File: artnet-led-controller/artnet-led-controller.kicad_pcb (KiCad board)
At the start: 2 copper layers, 100 x 70 mm, 84 parts, among them J1 USB4125-GF-A, J10 SWD_DEBUG, J2 HR911105A, J3 VBAT JST-PH-2, J5 LED_OUT_1, J6 LED_OUT_2, J7 LED_OUT_3, J8 LED_OUT_4, J9 OLED_SSD1306, SW1 SW_Push, SW2 SW_Push, SW3 SW_Push, SW4 SW_Push, U1 RP2354A, U3 W5500, U4 SN74AHCT125, U5 TP4056, U6 MT3608, U7 AMS1117-3.3, Y1 12MHz, Y2 25MHz

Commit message: Add netlist extraction and PCB pad net assignment
gen_schematic.py now exports netlist.json mapping each ref to its
pad-to-net assignments. gen_pcb.py loads this and injects (net N "name")
into every pad block so the board is routable with freerouting.
Also fixes pin_ep sign bug (cy+py -> cy-py) in schematic generator.

Co-Authored-By: Claude Sonnet 4.6 <noreply@anthropic.com>
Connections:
- C10 pad 1: (no net) -> GND
- C10 pad 2: (no net) -> VREG_1V1
- C2 pad 1: (no net) -> GND
- C2 pad 2: (no net) -> RP_XIN
- C3 pad 1: (no net) -> GND
- C3 pad 2: (no net) -> RP_XOUT
- C31 pad 1: (no net) -> VUSB
- C31 pad 2: (no net) -> GND
- C32 pad 1: (no net) -> VUSB
- C32 pad 2: (no net) -> GND
- C33 pad 1: (no net) -> VBAT
- C33 pad 2: (no net) -> GND
- C34 pad 1: (no net) -> VCC5V
- C34 pad 2: (no net) -> GND
- C35 pad 1: (no net) -> VCC5V
- C35 pad 2: (no net) -> GND
- C36 pad 1: (no net) -> VCC3V3
- C36 pad 2: (no net) -> GND
- C37 pad 1: (no net) -> VCC3V3
- C37 pad 2: (no net) -> GND
- C38 pad 1: (no net) -> VCC3V3
- C38 pad 2: (no net) -> GND
- C39 pad 1: (no net) -> VCC3V3
- C39 pad 2: (no net) -> GND
- C4 pad 1: (no net) -> GND
- C4 pad 2: (no net) -> W5_VDD
- C40 pad 1: (no net) -> VCC3V3
- C40 pad 2: (no net) -> GND
- C41 pad 1: (no net) -> VCC3V3
- C41 pad 2: (no net) -> GND
- C42 pad 1: (no net) -> VCC3V3
- C42 pad 2: (no net) -> GND
- C43 pad 1: (no net) -> VCC3V3
- C43 pad 2: (no net) -> GND
- C44 pad 1: (no net) -> VCC3V3
- C44 pad 2: (no net) -> GND
- C45 pad 1: (no net) -> VCC3V3
- C45 pad 2: (no net) -> GND
- C46 pad 1: (no net) -> VCC3V3
- C46 pad 2: (no net) -> GND
- C47 pad 1: (no net) -> VCC3V3
- C47 pad 2: (no net) -> GND
- C48 pad 1: (no net) -> VCC3V3
- C48 pad 2: (no net) -> GND
- C49 pad 1: (no net) -> VCC3V3
- C49 pad 2: (no net) -> GND
- C5 pad 1: (no net) -> GND
- C5 pad 2: (no net) -> W5_XTAL1
- C50 pad 1: (no net) -> VCC3V3
- C50 pad 2: (no net) -> GND
- C51 pad 1: (no net) -> VCC3V3
- C51 pad 2: (no net) -> GND
- C52 pad 1: (no net) -> VCC5V
- C52 pad 2: (no net) -> GND
- C6 pad 1: (no net) -> GND
- C6 pad 2: (no net) -> W5_XTAL2
- C7 pad 1: (no net) -> GND
- C7 pad 2: (no net) -> VREG_1V1
- C8 pad 1: (no net) -> GND
- C8 pad 2: (no net) -> VREG_AVDD
- C9 pad 1: (no net) -> GND
- C9 pad 2: (no net) -> VREG_1V1
- D1 pad 1: (no net) -> VCC5V
- D1 pad 2: (no net) -> VBOOST_RAW
- D2 pad 1: (no net) -> GND
- D2 pad 2: (no net) -> CHRG_STAT
- J1 pad A12: (no net) -> GND
- J1 pad A5: (no net) -> USB_CC1
- J1 pad B12: (no net) -> GND
- J1 pad B5: (no net) -> USB_CC2
- J10 pad 1: (no net) -> SWCLK
- J10 pad 2: (no net) -> SWDIO
- J10 pad 3: (no net) -> GND
- J2 pad 11: (no net) -> ETH_TXP
- J2 pad 12: (no net) -> ETH_TXN
- J2 pad 4: (no net) -> GND
- J2 pad 5: (no net) -> GND
- J2 pad 7: (no net) -> VCC3V3
- J2 pad 8: (no net) -> ETH_CT1
- J2 pad 9: (no net) -> ETH_CT2
- J3 pad 1: (no net) -> VBAT
- J3 pad 2: (no net) -> GND
- J5 pad 1: (no net) -> GND
- J5 pad 2: (no net) -> LED1_DATA_5V
- J5 pad 3: (no net) -> VCC5V
- J6 pad 1: (no net) -> GND
- J6 pad 2: (no net) -> LED2_DATA_5V
- J6 pad 3: (no net) -> VCC5V
- J7 pad 1: (no net) -> GND
- J7 pad 2: (no net) -> LED3_DATA_5V
- J7 pad 3: (no net) -> VCC5V
- J8 pad 1: (no net) -> GND
- J8 pad 2: (no net) -> LED4_DATA_5V
- J8 pad 3: (no net) -> VCC5V
- J9 pad 1: (no net) -> VCC3V3
- J9 pad 2: (no net) -> GND
- J9 pad 3: (no net) -> I2C_SCL
- J9 pad 4: (no net) -> I2C_SDA
- L1 pad 1: (no net) -> VBOOST_RAW
- L1 pad 2: (no net) -> MT3608_SW
- L2 pad 1: (no net) -> VREG_1V1
- L2 pad 2: (no net) -> VREG_LX
- R1 pad 1: (no net) -> MT3608_FB
- R1 pad 2: (no net) -> VCC5V
- R10 pad 1: (no net) -> USB_DM_MCU
- R10 pad 2: (no net) -> USB_DM
- R11 pad 1: (no net) -> GND
- R11 pad 2: (no net) -> W5500_EXRES0
- R12 pad 1: (no net) -> GND
- R12 pad 2: (no net) -> W5500_RCLK
- R13 pad 1: (no net) -> W5500_EXRES1
- R13 pad 2: (no net) -> VCC3V3
- R14 pad 1: (no net) -> SPI_MISO
- R14 pad 2: (no net) -> VCC3V3
- R15 pad 1: (no net) -> SPI_CS
- R15 pad 2: (no net) -> VCC3V3
- R16 pad 1: (no net) -> W5500_RST
- R16 pad 2: (no net) -> VCC3V3
- R17 pad 1: (no net) -> ETH_CT1
- R17 pad 2: (no net) -> VCC3V3
- R18 pad 1: (no net) -> ETH_CT2
- R18 pad 2: (no net) -> VCC3V3
- R19 pad 1: (no net) -> I2C_SCL
- R19 pad 2: (no net) -> VCC3V3
- R2 pad 1: (no net) -> GND
- R2 pad 2: (no net) -> MT3608_FB
- R20 pad 1: (no net) -> I2C_SDA
- R20 pad 2: (no net) -> VCC3V3
- R21 pad 1: (no net) -> BTN1
- R21 pad 2: (no net) -> VCC3V3
- R22 pad 1: (no net) -> BTN2
- R22 pad 2: (no net) -> VCC3V3
- R23 pad 1: (no net) -> VREG_AVDD
- R23 pad 2: (no net) -> VCC3V3
- R24 pad 1: (no net) -> USB_BOOT_SW
- R24 pad 2: (no net) -> USB_BOOT
- R3 pad 1: (no net) -> GND
- R3 pad 2: (no net) -> TP4056_PROG
- R4 pad 1: (no net) -> GND
- R4 pad 2: (no net) -> USB_CC1
- R5 pad 1: (no net) -> GND
- R5 pad 2: (no net) -> USB_CC2
- R6 pad 2: (no net) -> CHRG_STAT
- R7 pad 1: (no net) -> CHRG_STAT
- R7 pad 2: (no net) -> VCC3V3
- R8 pad 1: (no net) -> RP_RUN
- R8 pad 2: (no net) -> VCC3V3
- R9 pad 1: (no net) -> USB_DP_MCU
- R9 pad 2: (no net) -> USB_DP
- SW1 pad 1: (no net) -> BTN1
- SW1 pad 2: (no net) -> GND
- SW2 pad 1: (no net) -> BTN2
- SW2 pad 2: (no net) -> GND
- SW3 pad 1: (no net) -> RP_RUN
- SW3 pad 2: (no net) -> GND
- SW4 pad 1: (no net) -> USB_BOOT_SW
- SW4 pad 2: (no net) -> GND
- U1 pad 1: (no net) -> VCC3V3
- U1 pad 11: (no net) -> VCC3V3
- U1 pad 2: (no net) -> LED1_DATA_3V3
- U1 pad 20: (no net) -> VCC3V3
- U1 pad 21: (no net) -> RP_XIN
- U1 pad 22: (no net) -> RP_XOUT
- U1 pad 23: (no net) -> VREG_1V1
- U1 pad 24: (no net) -> SWCLK
- U1 pad 25: (no net) -> SWDIO
- U1 pad 26: (no net) -> RP_RUN
- U1 pad 27: (no net) -> SPI_MISO
- U1 pad 28: (no net) -> SPI_CS
- U1 pad 29: (no net) -> SPI_SCK
- U1 pad 3: (no net) -> LED2_DATA_3V3
- U1 pad 30: (no net) -> VCC3V3
- U1 pad 31: (no net) -> SPI_MOSI
- U1 pad 32: (no net) -> W5500_INT
- U1 pad 33: (no net) -> W5500_RST
- U1 pad 34: (no net) -> BTN1
- U1 pad 35: (no net) -> BTN2
- U1 pad 38: (no net) -> VCC3V3
- U1 pad 39: (no net) -> VREG_1V1
- U1 pad 4: (no net) -> LED3_DATA_3V3
- U1 pad 44: (no net) -> VCC3V3
- U1 pad 45: (no net) -> VCC3V3
- U1 pad 46: (no net) -> VREG_AVDD
- U1 pad 47: (no net) -> GND
- U1 pad 48: (no net) -> VREG_LX
- U1 pad 49: (no net) -> VCC3V3
- U1 pad 5: (no net) -> LED4_DATA_3V3
- U1 pad 50: (no net) -> VREG_1V1
- U1 pad 51: (no net) -> USB_DM_MCU
- U1 pad 52: (no net) -> USB_DP_MCU
- U1 pad 53: (no net) -> VCC3V3
- U1 pad 54: (no net) -> VCC3V3
- U1 pad 6: (no net) -> VREG_1V1
- U1 pad 60: (no net) -> USB_BOOT
- U1 pad 61: (no net) -> GND
- U1 pad 7: (no net) -> I2C_SDA
- U1 pad 8: (no net) -> I2C_SCL
- U3 pad 10: (no net) -> W5500_EXRES0
- U3 pad 11: (no net) -> ETH_TXP
- U3 pad 12: (no net) -> ETH_TXN
- U3 pad 13: (no net) -> ETH_RXN
- U3 pad 14: (no net) -> ETH_RXP
- U3 pad 15: (no net) -> W5_XTAL1
- U3 pad 16: (no net) -> W5_XTAL2
- U3 pad 19: (no net) -> VCC3V3
- U3 pad 20: (no net) -> VCC3V3
- U3 pad 21: (no net) -> SPI_MISO
- U3 pad 22: (no net) -> SPI_MOSI
- U3 pad 23: (no net) -> SPI_SCK
- U3 pad 24: (no net) -> SPI_CS
- U3 pad 25: (no net) -> VCC3V3
- U3 pad 26: (no net) -> W5_VDD
- U3 pad 27: (no net) -> W5500_INT
- U3 pad 28: (no net) -> W5500_RST
- U3 pad 32: (no net) -> GND
- U3 pad 5: (no net) -> W5500_EXRES1
- U3 pad 6: (no net) -> W5500_EXRES1
- U3 pad 7: (no net) -> VCC3V3
- U3 pad 8: (no net) -> GND
- U3 pad 9: (no net) -> W5500_RCLK
- U4 pad 1: (no net) -> GND
- U4 pad 10: (no net) -> LED3_DATA_3V3
- U4 pad 11: (no net) -> LED4_DATA_5V
- U4 pad 12: (no net) -> GND
- U4 pad 13: (no net) -> LED4_DATA_3V3
- U4 pad 14: (no net) -> VCC5V
- U4 pad 2: (no net) -> LED1_DATA_3V3
- U4 pad 3: (no net) -> LED1_DATA_5V
- U4 pad 4: (no net) -> GND
- U4 pad 5: (no net) -> LED2_DATA_3V3
- U4 pad 6: (no net) -> LED2_DATA_5V
- U4 pad 7: (no net) -> GND
- U4 pad 8: (no net) -> LED3_DATA_5V
- U4 pad 9: (no net) -> GND
- U5 pad 1: (no net) -> GND
- U5 pad 2: (no net) -> TP4056_PROG
- U5 pad 3: (no net) -> GND
- U5 pad 4: (no net) -> VUSB
- U5 pad 5: (no net) -> VBAT
- U5 pad 6: (no net) -> CHRG_STAT
- U5 pad 7: (no net) -> STDBY_STAT
- U5 pad 8: (no net) -> VUSB
- U6 pad 1: (no net) -> VBAT
- U6 pad 2: (no net) -> GND
- U6 pad 3: (no net) -> VCC5V
- U6 pad 4: (no net) -> MT3608_FB
- U6 pad 5: (no net) -> MT3608_SW
- U7 pad 1: (no net) -> GND
- U7 pad 2: (no net) -> VCC3V3
- U7 pad 3: (no net) -> VCC5V
- Y1 pad 1: (no net) -> RP_XIN
- Y1 pad 2: (no net) -> RP_XOUT
- Y2 pad 1: (no net) -> W5_XTAL1
- Y2 pad 2: (no net) -> W5_XTAL2

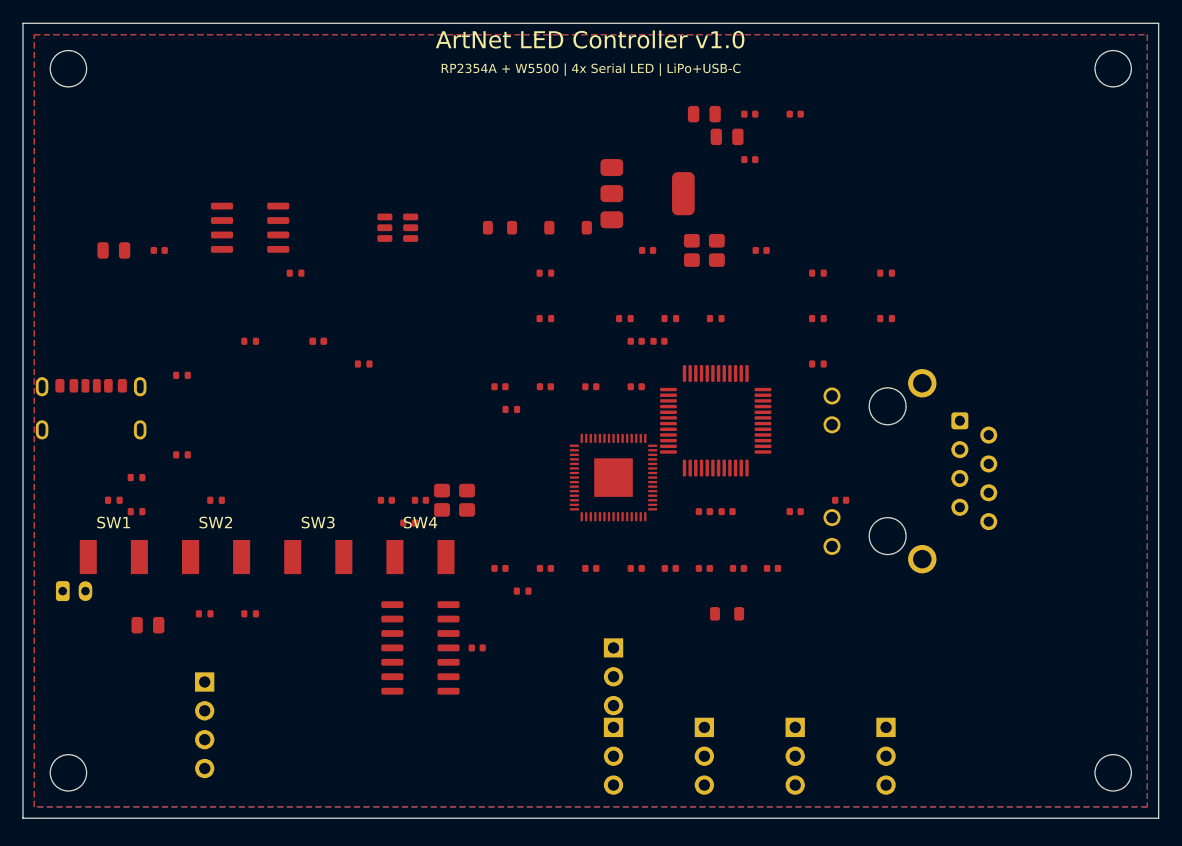
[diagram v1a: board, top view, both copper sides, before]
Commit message: Switch to 4-layer stackup with inner GND and VCC planes
Move to a 4-layer JLCPCB stackup: F.Cu/B.Cu for signals, In1.Cu as
VCC3V3 plane with a VCC5V island over the power-input column, In2.Cu
as a solid GND plane. Reworked component placement (edge-facing jacks,
courtyard-safe clusters) to improve routability.

Freerouting CLI cannot exploit inner planes (its DSN parser rejects
'(type power NET)'), so signal autorouting currently requires manual
completion in KiCad's interactive router.

Co-Authored-By: Claude Sonnet 4.6 <noreply@anthropic.com>
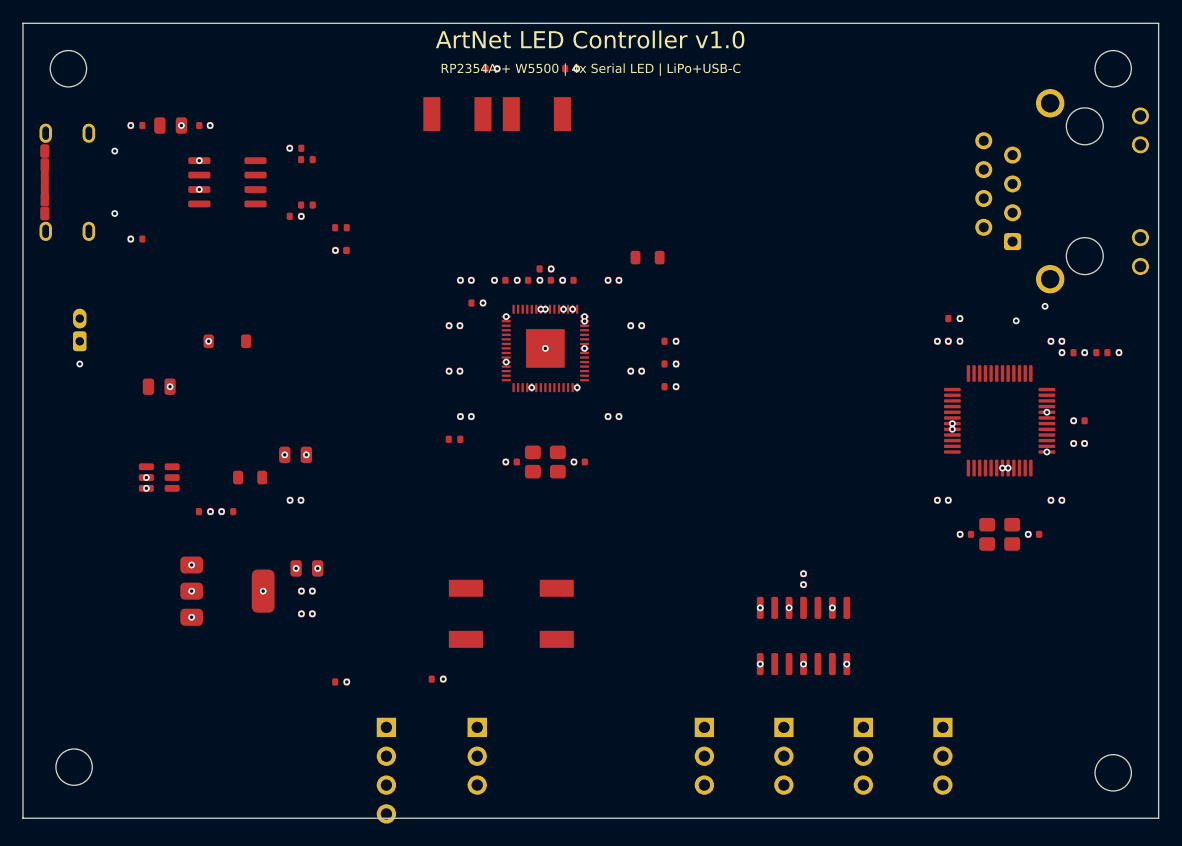
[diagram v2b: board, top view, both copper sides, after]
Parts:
- moved C38 61.5 mm to (25.0, 52.0)
- moved C37 57.3 mm to (25.0, 50.0)
- moved C36 53.2 mm to (25.0, 48.0)
- moved U7 50.9 mm to (18.0, 50.0)
- moved R21 50.5 mm to (41.2, 4.00)
- moved C35 50.0 mm to (24.0, 42.0)
- moved SW1 49.4 mm to (38.2, 8.00)
- moved R22 49.2 mm to (48.2, 4.00)
- moved SW2 48.2 mm to (45.2, 8.00)
- moved C34 47.2 mm to (24.0, 38.0)
- moved C5 37.5 mm to (83.0, 45.0)
- moved R1 36.6 mm to (16.0, 43.0)
- moved Y2 36.1 mm to (86.0, 45.0)
- moved C48 35.0 mm to (91.0, 28.0)
- moved C10 34.9 mm to (42.0, 22.6)
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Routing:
- net VCC5V: vias 0 -> 12
- net VCC3V3: vias 0 -> 47
- net GND: vias 0 -> 62
- added copper zone on In2.Cu, net GND
- added copper zone on In1.Cu, net VCC3V3
- added copper zone on In1.Cu, net VCC5V
- removed copper zone on B.Cu, net GND
- removed copper zone on F.Cu, net GND
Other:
- copper layers 2 -> 4
